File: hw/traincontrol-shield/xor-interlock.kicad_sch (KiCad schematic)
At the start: 0 parts

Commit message: Phase 3+4 complete: implement all 8 schematics, fix KiCad 9 lib embedding
All 7 sub-sheets and top-level sheet fully implemented and validated with
kicad-cli (exit 0 on all 8 files).

Key fixes to lib_sym_entry() in generator scripts:
- Sub-symbol names must NOT include library prefix (KiCad 9 parser requirement)
- Local KiCad 6 library symbols upgraded inline: remove (id N) from properties,
  strip stroke colors, fix bare 'hide', add exclude_from_sim + embedded_fonts
- Derived symbols (MOC3021M extends MOC3010M) flattened by copying base
  graphics into derived, removing (extends ...) for standalone embedding

Validated: kicad-cli sch export netlist exits 0 for all 8 .kicad_sch files.

Co-Authored-By: Claude Sonnet 4.6 <noreply@anthropic.com>
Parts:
- added C10, C11: 100nF, Capacitor_SMD:C_0603_1608Metric, symbol Device:C
- added U3: 74LVC1G86, Package_TO_SOT_SMD:SOT-23-5, symbol 74xGxx:74LVC1G86
- added U4: 74LVC2G08, Package_TO_SOT_SMD:SOT-363_SC-70-6, symbol 74xGxx:74LVC2G08
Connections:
- new net +3V3: C10.2, C11.2, U3.3 (GND), U4.4 (GND)
- new net CTRL_A: U3.2, U4.1
- new net CTRL_B: U3.1, U4.5
- new net GND: C10.1, C11.1, U3.5 (VCC), U4.8 (VCC)
- new net PHASE_A: U4.7
- new net PHASE_B: U4.3
- new net XOR_OUT: U3.4, U4.2, U4.6
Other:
- title: Traincontrol Shield — XOR Interlock -> XOR Interlock

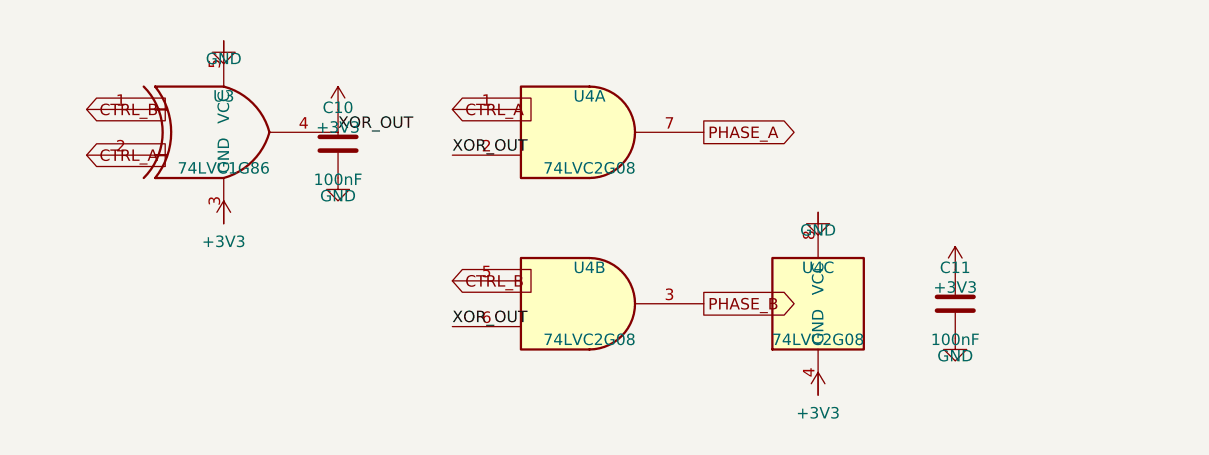
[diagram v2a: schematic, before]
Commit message: Add 2.54mm wire stubs to all power and global label connections
Power symbols (GND/+V) and global labels were placed directly on
component pins, making connections invisible in KiCad GUI. Add a
2.54mm stub wire between each component pin and power symbol/label
so connections are visually distinct. GND stubs go down (+y), +V
stubs go up (-y), label stubs go horizontally away from pin.
PWR_FLAG symbols are excluded (already have explicit wires).

All 8 schematics validate with kicad-cli exit 0.

Co-Authored-By: Claude Sonnet 4.6 <noreply@anthropic.com>
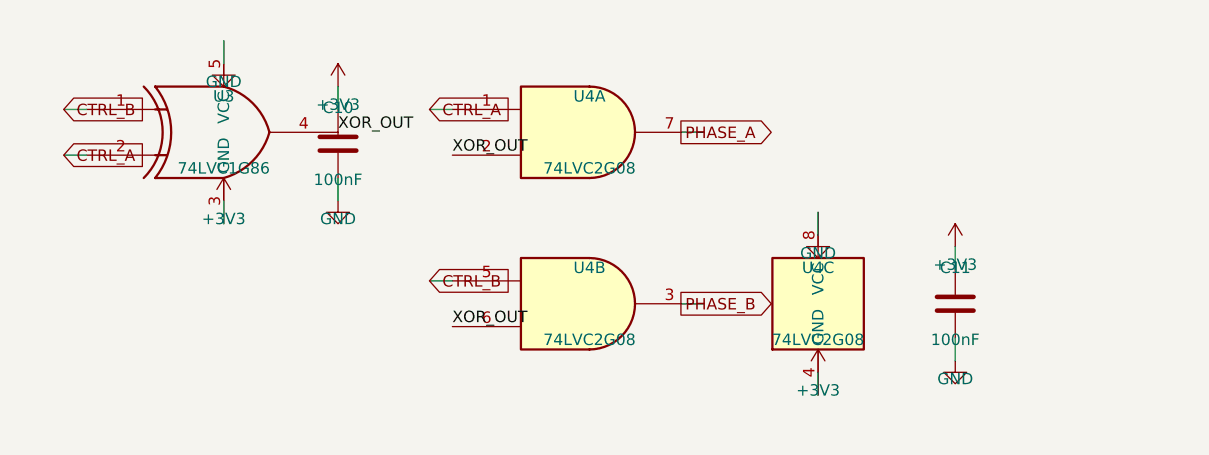
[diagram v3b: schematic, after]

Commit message: Add hierarchical ports to all sub-sheets and top-level connections
Replace inter-sheet global_label elements with hierarchical_label in all
sub-sheets, so each sheet exports visible ports on its sheet box symbol
in the top-level. Add matching (pin ...) entries to every sheet block in
the top-level. Connect all sheet pins with bidirectional global_labels in
the inter-column gap (x=105..120) so named nets auto-join.

Port counts per sub-sheet:
  power-supply:       2  (AC_IN, AC_RTN)
  zero-crossing:      3  (AC_IN, AC_RTN, ZC_OUT)
  xor-interlock:      6  (CTRL_A×2, CTRL_B×2, PHASE_A, PHASE_B)
  opto-triac-drive:   6  (PHASE_A, PHASE_B, AC_RTN×2, TRIAC_A_GATE, TRIAC_B_GATE)
  triacs-snubbers:   12  (AC_RTN×2, WINDING_A×3, WINDING_B×3, TRIAC_A_GATE, TRIAC_B_GATE)
  rail-voltage-sense: 1  (VSENSE)
  mcu:                4  (CTRL_A, CTRL_B, ZC_OUT, VSENSE)

All 8 schematics validate: kicad-cli exit 0.
Fix: correct KiCad 9 keyword is `hierarchical_label`, not `hier_label`.

Co-Authored-By: Claude Sonnet 4.6 <noreply@anthropic.com>
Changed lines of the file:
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@@
 		(stroke (width 0) (type solid))
 	)
-	(global_label "CTRL_A"
+	(hierarchical_label "CTRL_A"
 		(shape input)
 		(at 45.72 92.71 0)
@@
 		(stroke (width 0) (type solid))
 	)
-	(global_label "CTRL_B"
+	(hierarchical_label "CTRL_B"
 		(shape input)
 		(at 45.72 87.63 0)
@@
 		(stroke (width 0) (type solid))
 	)
-	(global_label "CTRL_A"
+	(hierarchical_label "CTRL_A"
 		(shape input)
 		(at 86.36 87.63 0)
@@
 		(stroke (width 0) (type solid))
 	)
-	(global_label "CTRL_B"
+	(hierarchical_label "CTRL_B"
 		(shape input)
 		(at 86.36 106.68 0)
@@
 		(stroke (width 0) (type solid))
 	)
-	(global_label "PHASE_A"
+	(hierarchical_label "PHASE_A"
 		(shape output)
 		(at 114.3 90.17 0)
@@
 		(stroke (width 0) (type solid))
 	)
-	(global_label "PHASE_B"
+	(hierarchical_label "PHASE_B"
 		(shape output)
 		(at 114.3 109.22 0)

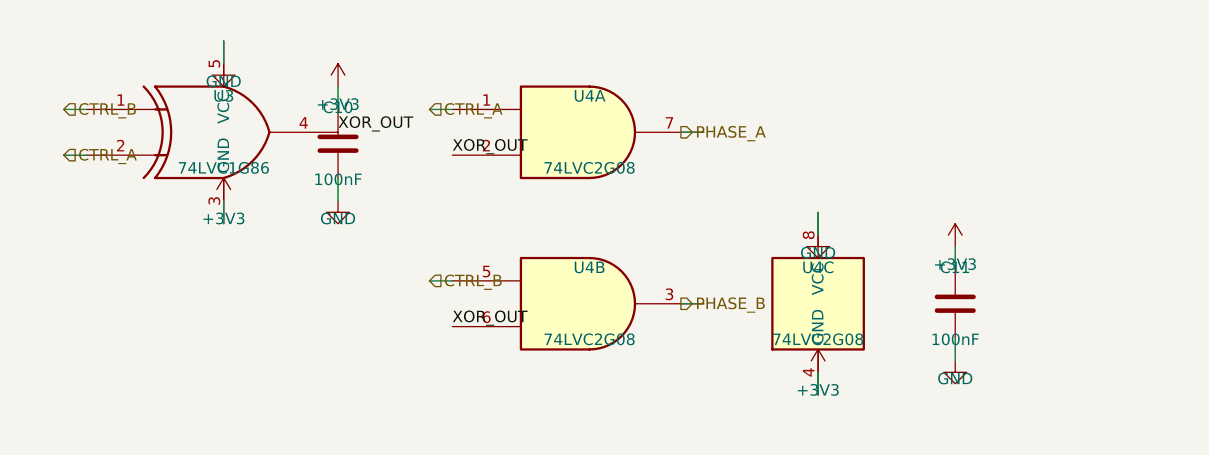
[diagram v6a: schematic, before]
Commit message: Disperse component layout and triple wire stub length across all sheets
- STUB: 2.54 → 7.62 mm (3×) in all three generator scripts
- Inter-component spacing doubled in power-supply, MCU, and logic sheets
- Top-level inter-column gap widened (LX 120 → 130 mm) to avoid label collision
- Sheet frame heights made variable per pin count (20–35 mm)
- Right-column sheet x-origin and connector J4/J5/J6 x-positions updated accordingly
- All 8 sheets regenerated and validated with kicad-cli

Co-Authored-By: Claude Sonnet 4.6 <noreply@anthropic.com>
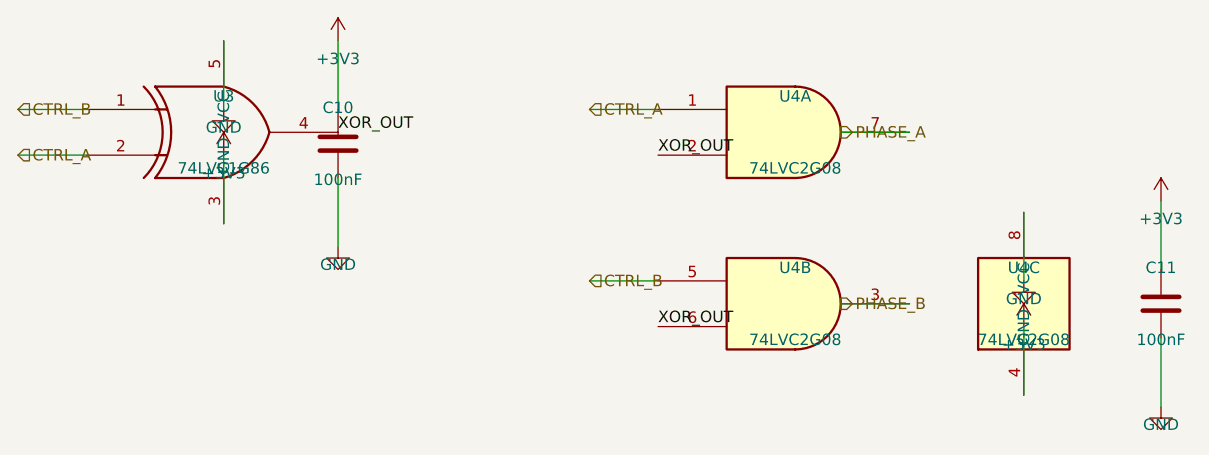
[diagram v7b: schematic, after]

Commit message: Fix U4 footprint: SOT-363_SC-70-6 (6-pin) → VSSOP-8_2.3x2mm_P0.5mm (8-pin)
74LVC2G08 has 8 pins (dual AND gate + VCC/GND); SOT-363 only has 6 pads.
Correct footprint is VSSOP-8 per the symbol's ki_fp_filters (SSOP*/VSSOP*).

Co-Authored-By: Claude Sonnet 4.6 <noreply@anthropic.com>
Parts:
- U4: footprint Package_TO_SOT_SMD:SOT-363_SC-70-6 -> Package_SO:VSSOP-8_2.3x2mm_P0.5mm
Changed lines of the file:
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@@
 			(effects (font (size 1.27 1.27)))
 		)
-		(property "Footprint" "Package_TO_SOT_SMD:SOT-363_SC-70-6"
+		(property "Footprint" "Package_SO:VSSOP-8_2.3x2mm_P0.5mm"
 			(at 127.0 90.17 0)
 			(effects (font (size 1.27 1.27)) (hide yes))
@@
 			(effects (font (size 1.27 1.27)))
 		)
-		(property "Footprint" "Package_TO_SOT_SMD:SOT-363_SC-70-6"
+		(property "Footprint" "Package_SO:VSSOP-8_2.3x2mm_P0.5mm"
 			(at 127.0 109.22 0)
 			(effects (font (size 1.27 1.27)) (hide yes))
@@
 			(effects (font (size 1.27 1.27)))
 		)
-		(property "Footprint" "Package_TO_SOT_SMD:SOT-363_SC-70-6"
+		(property "Footprint" "Package_SO:VSSOP-8_2.3x2mm_P0.5mm"
 			(at 152.4 109.22 0)
 			(effects (font (size 1.27 1.27)) (hide yes))
